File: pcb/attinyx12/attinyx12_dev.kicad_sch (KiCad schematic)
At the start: 19 parts, among them J1 Conn_01x06, J2 Conn_01x03, J3 Conn_01x06, J4 Conn_01x06, J5 Conn_01x06, J6 USB_B_Micro, U1 ATtiny212-SS, U2 CH340C

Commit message: rename kicad project and dir
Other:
- company: erry Leumas -> Perry Leumas
- title: ATTiny212 Development Board -> ATtinyX12 Development Board
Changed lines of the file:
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@@
 	(paper "A")
 	(title_block
-		(title "ATTiny212 Development Board")
-		(company "erry Leumas")
+		(title "ATtinyX12 Development Board")
+		(company "Perry Leumas")
 	)
 	(junction

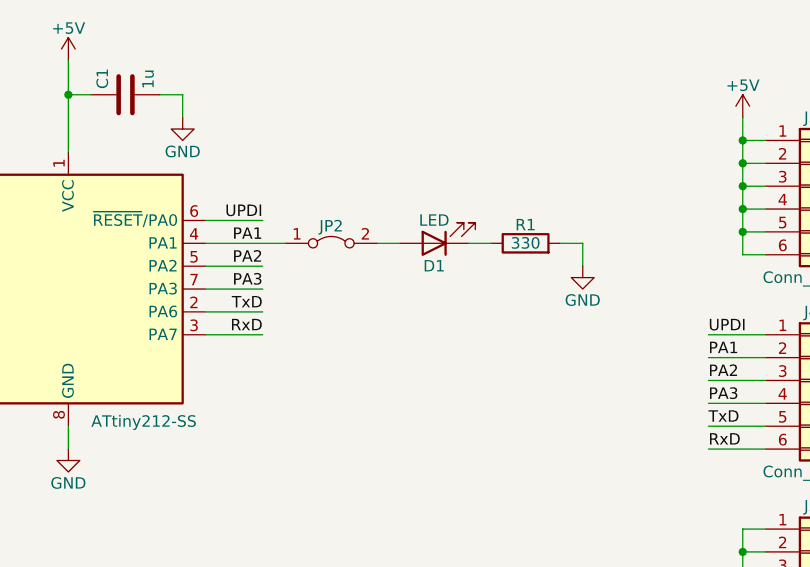
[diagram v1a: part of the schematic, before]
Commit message: schematic update
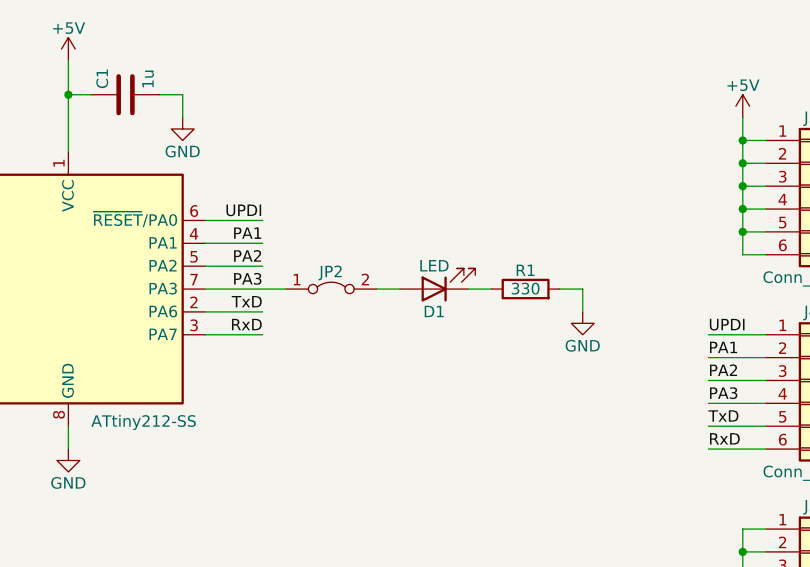
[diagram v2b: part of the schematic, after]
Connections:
- net PA1: no longer JP2.1 (A)
- net PA3: now also JP2.1 (A)
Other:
- moved on the sheet: D1, JP2, R1
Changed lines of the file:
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@@
 	(wire
 		(pts
+			(xy 143.51 96.52) (xy 149.86 96.52)
+		)
+		(stroke
+			(width 0)
+			(type default)
+		)
+	)
+	(wire
+		(pts
 			(xy 179.07 29.21) (xy 175.26 29.21)
 		)
@@
 	(wire
 		(pts
-			(xy 143.51 101.6) (xy 149.86 101.6)
+			(xy 143.51 101.6) (xy 152.4 101.6)
 		)
 		(stroke
@@
 	(wire
 		(pts
-			(xy 185.42 96.52) (xy 185.42 99.06)
+			(xy 185.42 101.6) (xy 185.42 104.14)
 		)
 		(stroke
@@
 	(wire
 		(pts
-			(xy 143.51 96.52) (xy 152.4 96.52)
-		)
-		(stroke
-			(width 0)
-			(type default)
-		)
-	)
-	(wire
-		(pts
 			(xy 128.27 80.01) (xy 130.81 80.01)
 		)
@@
 	(wire
 		(pts
-			(xy 182.88 96.52) (xy 185.42 96.52)
+			(xy 182.88 101.6) (xy 185.42 101.6)
 		)
 		(stroke
@@
 	(wire
 		(pts
-			(xy 172.72 96.52) (xy 175.26 96.52)
+			(xy 172.72 101.6) (xy 175.26 101.6)
 		)
 		(stroke
@@
 	(wire
 		(pts
-			(xy 162.56 96.52) (xy 165.1 96.52)
+			(xy 162.56 101.6) (xy 165.1 101.6)
 		)
 		(stroke
@@
 	(symbol
 		(lib_id "Jumper:Jumper_2_Bridged")
-		(at 157.48 96.52 0)
+		(at 157.48 101.6 0)
 		(unit 1)
 		(exclude_from_sim no)
@@
 		(dnp no)
 		(property "Reference" "JP2"
-			(at 157.48 94.615 0)
+			(at 157.48 99.695 0)
 			(effects
 				(font
@@
 		)
 		(property "Value" "Jumper_2_Bridged"
-			(at 157.48 99.06 0)
+			(at 157.48 104.14 0)
 			(effects
 				(font
@@
 		)
 		(property "Footprint" "Connector_PinHeader_2.54mm:PinHeader_1x02_P2.54mm_Vertical"
-			(at 157.48 96.52 0)
+			(at 157.48 101.6 0)
 			(effects
 				(font
@@
 		)
 		(property "Datasheet" "~"
-			(at 157.48 96.52 0)
+			(at 157.48 101.6 0)
 			(effects
 				(font
@@
 		)
 		(property "Description" ""
-			(at 157.48 96.52 0)
+			(at 157.48 101.6 0)
 			(effects
 				(font
@@
 	(symbol
 		(lib_id "Device:LED")
-		(at 168.91 96.52 180)
+		(at 168.91 101.6 180)
 		(unit 1)
 		(exclude_from_sim no)
@@
 		(dnp no)
 		(property "Reference" "D1"
-			(at 168.91 99.06 0)
+			(at 168.91 104.14 0)
 			(effects
 				(font
@@
 		)
 		(property "Value" "LED"
-			(at 168.91 93.98 0)
+			(at 168.91 99.06 0)
 			(effects
 				(font
@@
 		)
 		(property "Footprint" "LED_THT:LED_D3.0mm"
-			(at 168.91 96.52 0)
+			(at 168.91 101.6 0)
 			(effects
 				(font
@@
 		)
 		(property "Datasheet" "~"
-			(at 168.91 96.52 0)
+			(at 168.91 101.6 0)
 			(effects
 				(font
@@
 		)
 		(property "Description" ""
-			(at 168.91 96.52 0)
+			(at 168.91 101.6 0)
 			(effects
 				(font
@@
 	(symbol
 		(lib_id "Device:R")
-		(at 179.07 96.52 90)
+		(at 179.07 101.6 90)
 		(unit 1)
 		(exclude_from_sim no)
@@
 		(dnp no)
 		(property "Reference" "R1"
-			(at 179.07 94.488 90)
+			(at 179.07 99.568 90)
 			(effects
 				(font
@@
 		)
 		(property "Value" "330"
-			(at 179.07 96.52 90)
+			(at 179.07 101.6 90)
 			(effects
 				(font
@@
 		)
 		(property "Footprint" "Resistor_THT:R_Axial_DIN0207_L6.3mm_D2.5mm_P10.16mm_Horizontal"
-			(at 179.07 98.298 90)
+			(at 179.07 103.378 90)
 			(effects
 				(font
@@
 		)
 		(property "Datasheet" "~"
-			(at 179.07 96.52 0)
+			(at 179.07 101.6 0)
 			(effects
 				(font
@@
 		)
 		(property "Description" ""
-			(at 179.07 96.52 0)
+			(at 179.07 101.6 0)
 			(effects
 				(font
@@
 		)
 		(property "MPN" ""
-			(at 179.07 96.52 0)
+			(at 179.07 101.6 0)
 			(effects
 				(font
@@
 		)
 		(property "Manufacture" ""
-			(at 179.07 96.52 0)
+			(at 179.07 101.6 0)
 			(effects
 				(font
@@
 		)
 		(property "SPN" ""
-			(at 179.07 96.52 0)
+			(at 179.07 101.6 0)
 			(effects
 				(font
@@
 		)
 		(property "Supplier" ""
-			(at 179.07 96.52 0)
+			(at 179.07 101.6 0)
 			(effects
 				(font
@@
 		)
 		(property "Tolerance" ""
-			(at 179.07 96.52 0)
+			(at 179.07 101.6 0)
 			(effects
 				(font
@@
 		)
 		(property "Voltage" ""
-			(at 179.07 96.52 0)
+			(at 179.07 101.6 0)
 			(effects
 				(font
@@
 		)
 		(property "Power" ""
-			(at 179.07 96.52 0)
+			(at 179.07 101.6 0)
 			(effects
 				(font
@@
 	(symbol
 		(lib_id "power:GND")
-		(at 185.42 99.06 0)
+		(at 185.42 104.14 0)
 		(unit 1)
 		(exclude_from_sim no)
@@
 		(dnp no)
 		(property "Reference" "#PWR08"
-			(at 185.42 105.41 0)
+			(at 185.42 110.49 0)
 			(effects
 				(font
@@
 		)
 		(property "Value" "GND"
-			(at 185.42 102.87 0)
+			(at 185.42 107.95 0)
 			(effects
 				(font
@@
 		)
 		(property "Footprint" ""
-			(at 185.42 99.06 0)
+			(at 185.42 104.14 0)
 			(effects
 				(font
@@
 		)
 		(property "Datasheet" ""
-			(at 185.42 99.06 0)
+			(at 185.42 104.14 0)
 			(effects
 				(font
@@
 		)
 		(property "Description" ""
-			(at 185.42 99.06 0)
+			(at 185.42 104.14 0)
 			(effects
 				(font

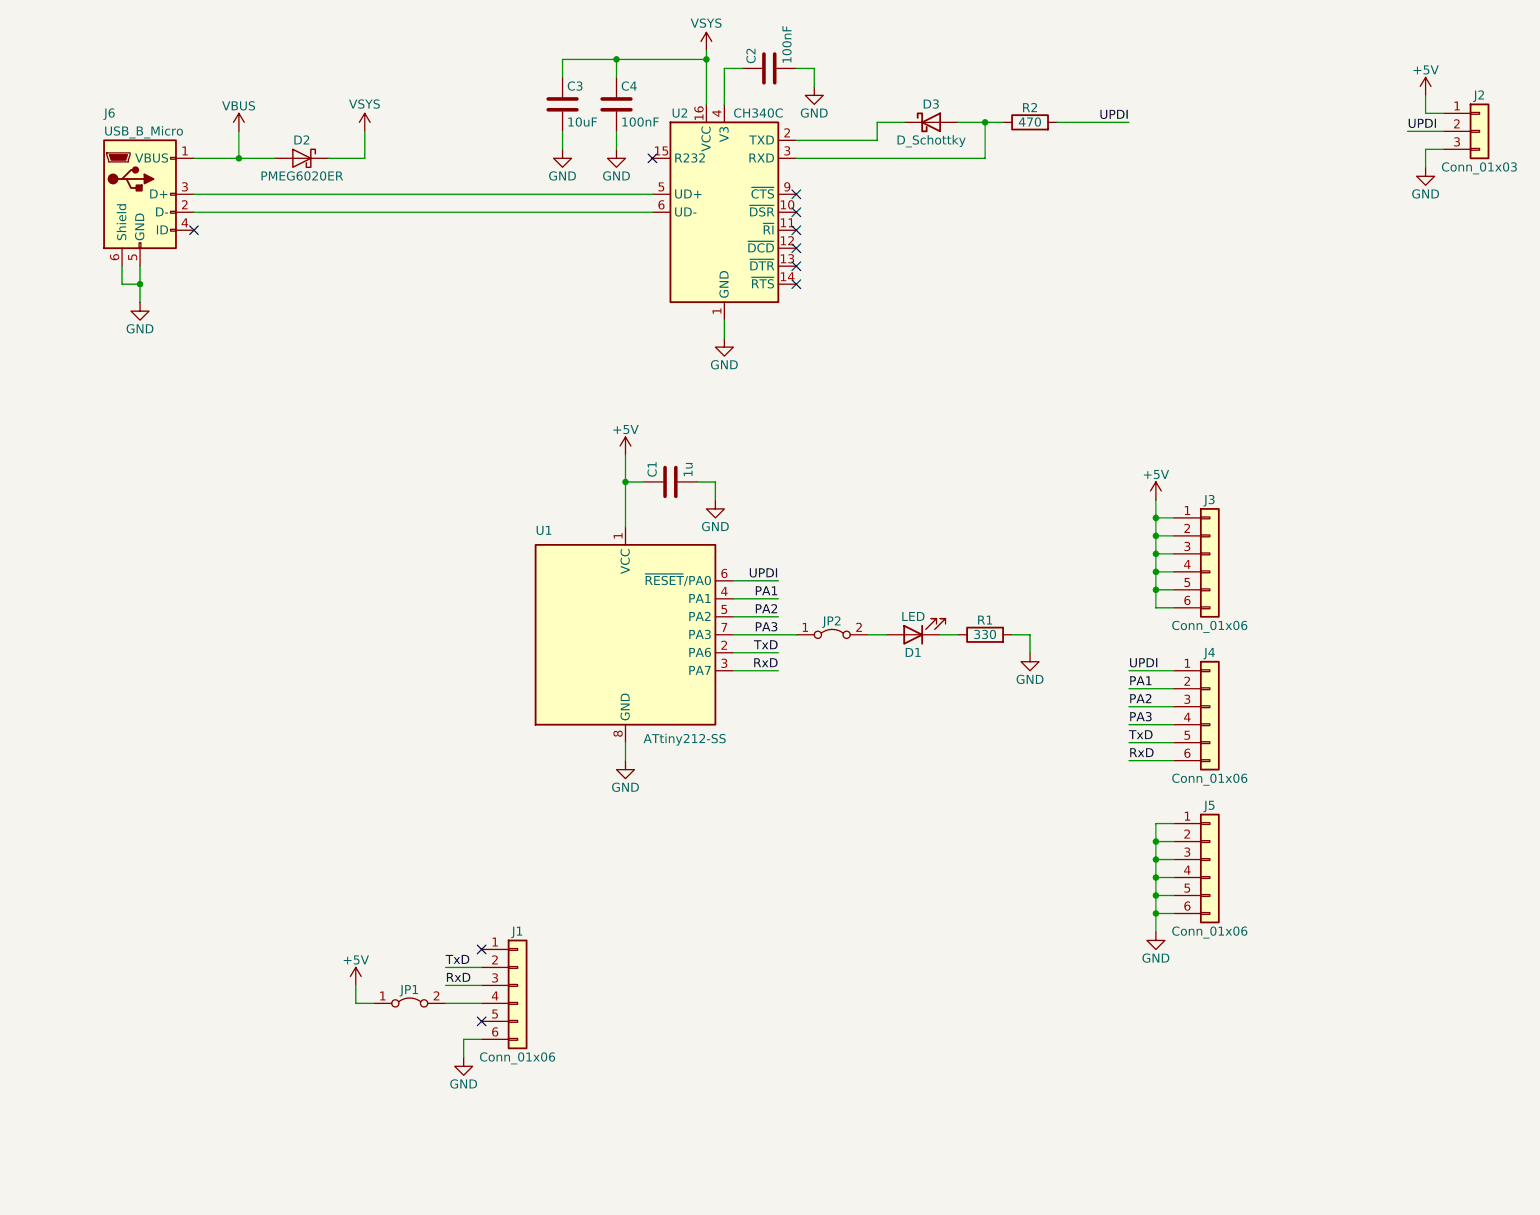
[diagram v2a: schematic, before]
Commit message: Update attinyx12_dev.kicad_sch
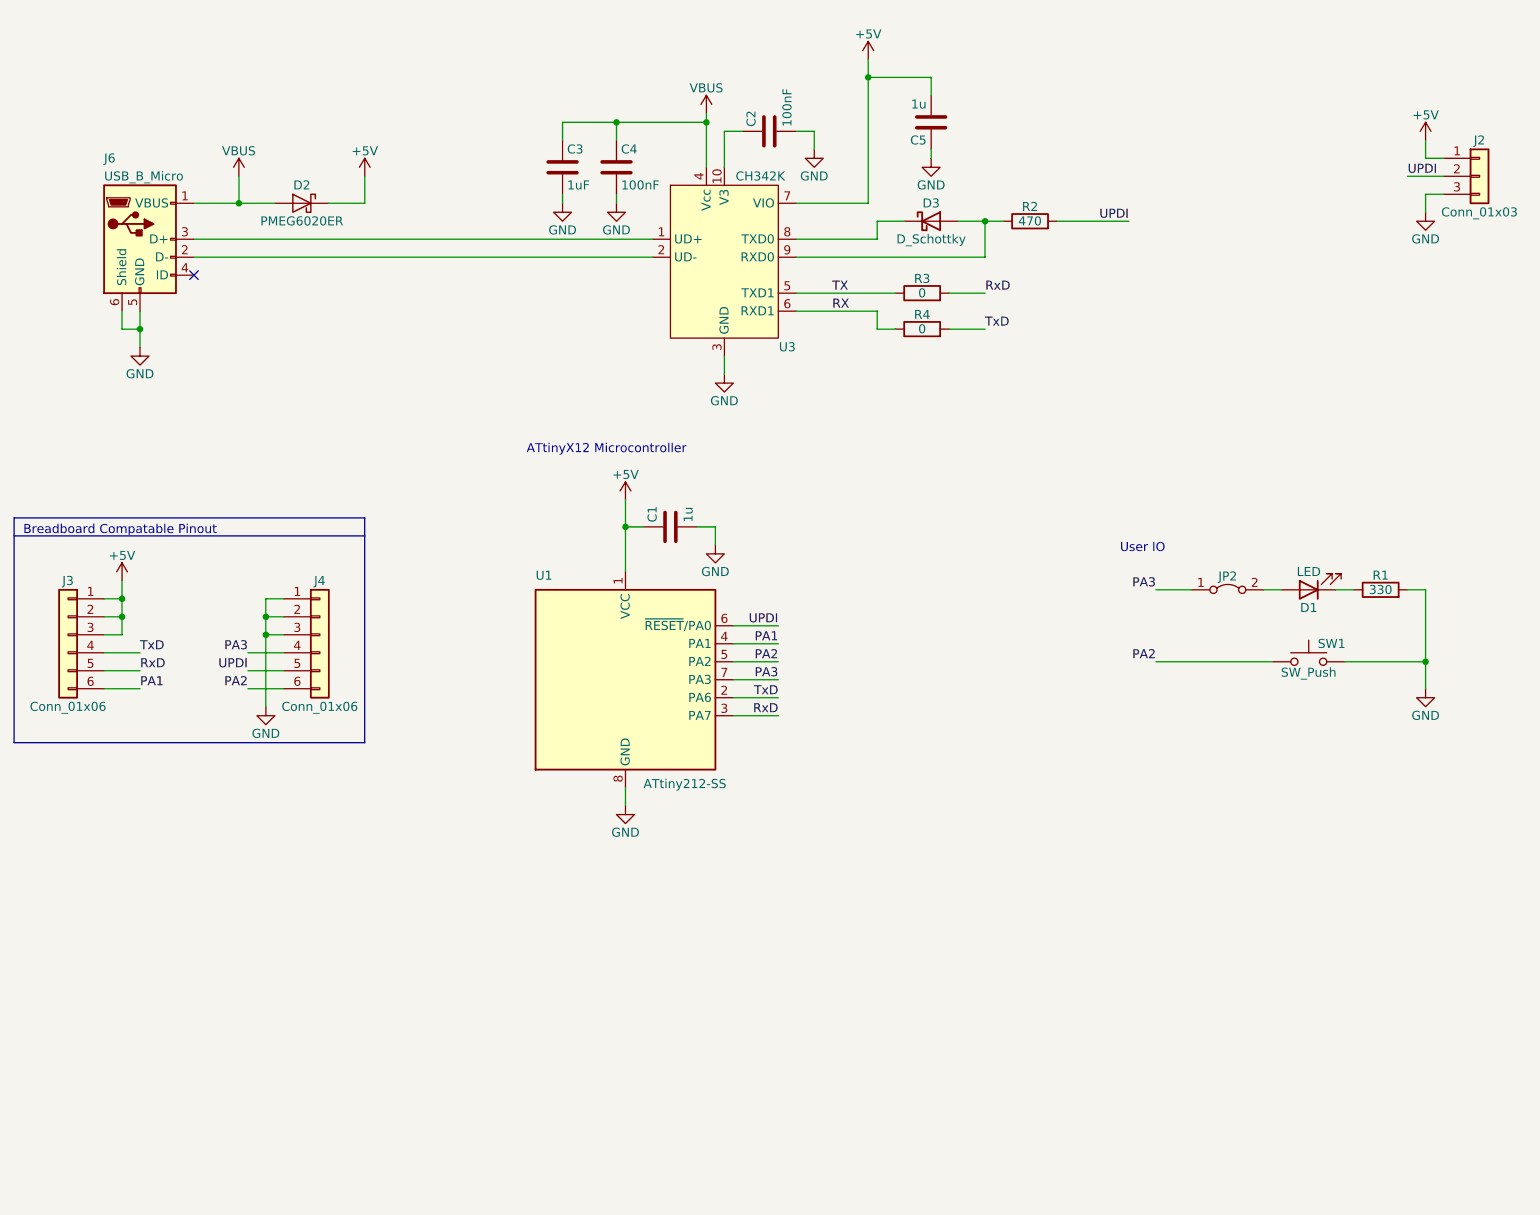
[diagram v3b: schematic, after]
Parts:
- removed J1, J5: Conn_01x06, Connector_PinHeader_2.54mm:PinHeader_1x06_P2.54mm_Vertical, symbol Connector_Generic:Conn_01x06
- removed JP1: Jumper_2_Bridged, Connector_PinHeader_2.54mm:PinHeader_1x02_P2.54mm_Vertical, symbol Jumper:Jumper_2_Bridged
- removed U2: CH340C, Package_SO:SOIC-16_3.9x9.9mm_P1.27mm, symbol Interface_USB:CH340C
- added C5: 1u, Capacitor_SMD:C_1210_3225Metric_Pad1.33x2.70mm_HandSolder, symbol Device:C
- added R3, R4: 0, symbol Device:R
- added SW1: SW_Push, symbol Switch:SW_Push
- added U3: CH342K, Package_SO:SSOP-10-1EP_3.9x4.9mm_P1mm_EP2.1x3.3mm, symbol pl_CH342:CH342K
- C3: value 10uF -> 1uF
- J3, J4: footprint Connector_PinHeader_2.54mm:PinHeader_1x06_P2.54mm_Vertical -> (none)
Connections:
- net +5V: now also D2.1 (K), C5.2, U3.7 (VIO); no longer J3.4 (Pin_4), J3.5 (Pin_5), J3.6 (Pin_6)
- net GND: now also J4.1 (Pin_1), J4.2 (Pin_2), J4.3 (Pin_3), C5.1, SW1.2, U3.11 (GND), U3.3 (GND)
- net PA1: now also J3.6 (Pin_6); no longer J4.2 (Pin_2)
- net PA2: now also J4.6 (Pin_6), SW1.1; no longer J4.3 (Pin_3)
- net RxD: now also J3.5 (Pin_5), R3.2; no longer J4.6 (Pin_6)
- net TxD: now also J3.4 (Pin_4), R4.2; no longer J4.5 (Pin_5)
- net UPDI: now also J4.5 (Pin_5); no longer J4.1 (Pin_1)
- net VBUS: now also C3.1, C4.1, U3.4 (Vcc)
- net at D3.2 (A), R2.1: now also U3.9 (RXD0)
- net at C2.1: now also U3.10 (V3)
- net at D3.1 (K): now also U3.8 (TXD0)
- net at J6.3 (D+): now also U3.1 (UD+)
- net at J6.2 (D-): now also U3.2 (UD-)
- removed net VSYS: C3.1, C4.1, D2.1 (K)
- new net RX: R4.1, U3.6 (RXD1)
- new net TX: R3.1, U3.5 (TXD1)
- no-connect marks 10 -> 1
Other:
- note added: "ATtinyX12 Microcontroller"
- note added: "Breadboard Compatable Pinout"
- note added: "User IO"
- moved on the sheet: C1, C2, C3, C4, D1, D2, D3, J2, J6, JP2, R1, R2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
